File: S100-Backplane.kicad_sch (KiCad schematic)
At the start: 84 parts, among them IC1 7805, IC2 LM4250, IC3 PTN78000AAH, IC4 15V D30V30F15, IC5 7.5V D36V50F7, J1 Barrel_Jack_MountingPin, K1 CONN_3, P1 CONN_3X2, P10 CONN_1, P11 CONN_1, P12 CONN_2, P2 CONN_13X2, P3 CONN_13X2, P4 CONN_13X2, P5 CONN_13X2, P6 CONN_1, P7 CONN_1, P8 CONN_1, P9 CONN_1, Q1 2N3906TF, Q2 2N3904TA, Q3 TIP29BG, Q4 TIP30CG, SW1 SW_PUSH, SW2 B12JH, U31 S100_FEMALE, U32 S100_FEMALE, U33 S100_FEMALE, U34 S100_FEMALE, U35 S100_FEMALE, U36 S100_FEMALE, U37 S100_FEMALE, U38 S100_FEMALE, U39 S100_FEMALE

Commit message: Rev 1
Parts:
- removed F1, F2, F3: FUSE, R5, symbol S100-Backplane-rescue:FUSE
- removed JP1, JP2, JP3: JUMPER, SIL-2, symbol S100-Backplane-rescue:JUMPER
- removed R12, R13, R14: 270, R3, symbol S100-Backplane-rescue:R
- added D4: LED, S100 Backplane:LEDV, symbol S100-Backplane-rescue:LED
- added F1, F3: MF-R050-2, samac:MFR0502, symbol SamacSym:MF-R050-2
- added F2: MF-R250-2, samac:MFR2502, symbol SamacSym:MF-R250-2
- added JP1, JP2, JP3: Jumper_3_Open, Connector_PinHeader_2.54mm:PinHeader_1x03_P2.54mm_Vertical, symbol Jumper:Jumper_3_Open
- added JP4: ~, Connector_PinHeader_2.54mm:PinHeader_1x02_P2.54mm_Vertical, symbol Jumper:Jumper_2_Open
- added RR11: 270, Connector_PinHeader_2.54mm:PinHeader_1x05_P2.54mm_Vertical, symbol S100-Backplane-rescue:RR9
- R11: value 270 -> 27
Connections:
- net +18_V: now also F3.2
- net +8_V: now also F2.2
- net -16_V: now also F1.2
- net /CLOCK: now also RR11.3
- net /POC: now also RR11.5
- net F+16V: now also F3.1
- net F+8V: now also F2.1, JP4.2 (B); no longer C1.1, IC1.VI, Q1.1 (E), Q3.2, R5.1
- net F-16V: now also F1.1
- net GND: now also R11.2, JP1.3 (B), JP2.3 (B), JP3.3 (B)
- net PROT(GND): now also JP3.1 (A); no longer P3.16 (P16), U31.70 (0_V4), U32.70 (0_V4), U33.70 (0_V4), U34.70 (0_V4), U35.70 (0_V4), U36.70 (0_V4), U37.70 (0_V4), U38.70 (0_V4), U39.70 (0_V4)
- net SHLTA: now also RR11.2; no longer R11.1
- net SSTACK: now also RR11.4
- net UNPROT(T5): now also JP1.1 (A); no longer P3.15 (P15), U31.20 (0_V1), U32.20 (0_V1), U33.20 (0_V1), U34.20 (0_V1), U35.20 (0_V1), U36.20 (0_V1), U37.20 (0_V1), U38.20 (0_V1), U39.20 (0_V1)
- net Vacc: now also D4.1 (A), RR11.1 (COM); no longer R11.2
- net /SSW_DSBL renamed /J_SSW_DSBL
- net /J_SSW_DSBL: now also JP2.2 (C); no longer RR6.2
- new net: D4.2 (K), R11.1
- new net J_F+8V: C1.1, IC1.VI, JP4.1 (A), Q1.1 (E), Q3.2, R5.1
- new net J_PROT(GND): JP3.2 (C), P3.16 (P16), U31.70 (0_V4), U32.70 (0_V4), U33.70 (0_V4), U34.70 (0_V4), U35.70 (0_V4), U36.70 (0_V4), U37.70 (0_V4), U38.70 (0_V4), U39.70 (0_V4)
- new net J_UNPROT(T5): JP1.2 (C), P3.15 (P15), U31.20 (0_V1), U32.20 (0_V1), U33.20 (0_V1), U34.20 (0_V1), U35.20 (0_V1), U36.20 (0_V1), U37.20 (0_V1), U38.20 (0_V1), U39.20 (0_V1)
- new net /SSW_DSBL: JP2.1 (A), RR6.2
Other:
- moved on the sheet: C1, C2, C3, C4, C5, C6, C7, C8, D2, IC1, IC2, P10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

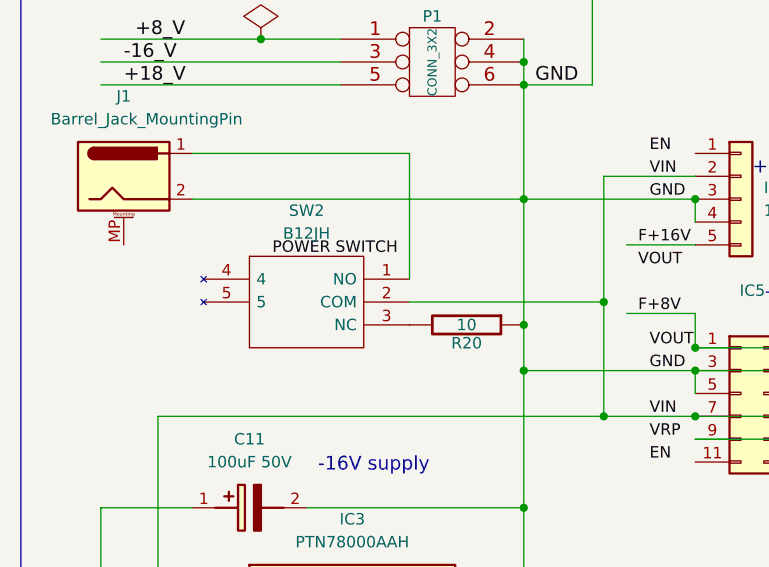
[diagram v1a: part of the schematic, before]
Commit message: R2
Updated SW2 power switch footprint to beefier part, E101MD1AQE.
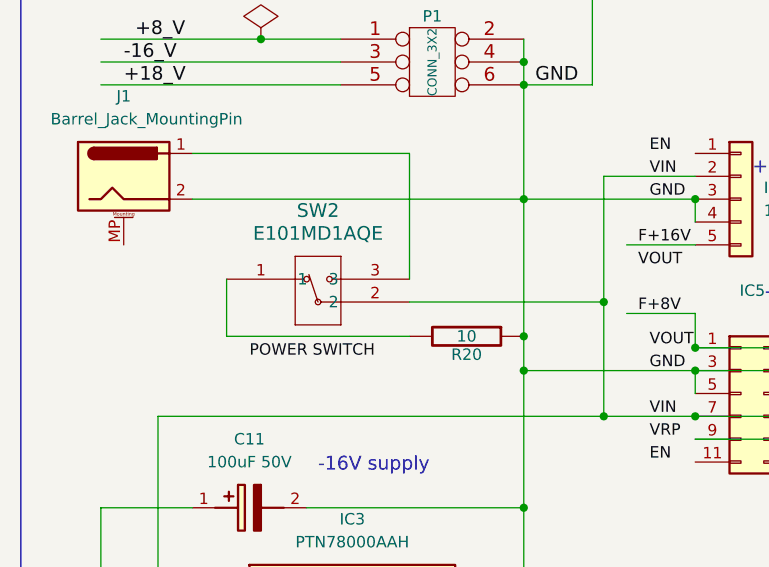
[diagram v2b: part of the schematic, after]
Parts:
- removed SW2: B12JH, B12JH, symbol SamacLib:B12JH
- added SW2: E101MD1AQE, SW_E1xxMD1AxE_CNK, symbol E101MD1AQE:E101MD1AQE
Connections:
- net VIN: now also SW2.2
- net at J1.1: now also SW2.3
- net at R20.2: now also SW2.1
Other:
- moved on the sheet: R20
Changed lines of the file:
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@@
   (junction (at 91.44 344.17) (diameter 0) (color 0 0 0 0)
   )
+  (junction (at 72.39 342.9) (diameter 0) (color 0 0 0 0)
+  )
   (junction (at 252.73 388.62) (diameter 0) (color 0 0 0 0)
   )
@@
   (junction (at 303.53 388.62) (diameter 0) (color 0 0 0 0)
   )
-  (junction (at 72.39 341.63) (diameter 0) (color 0 0 0 0)
-  )
   (junction (at 280.67 414.02) (diameter 0) (color 0 0 0 0)
   )
@@
     (stroke (width 0) (type default))
   )
-  (wire (pts (xy 72.39 341.63) (xy 72.39 346.71))
-    (stroke (width 0) (type default))
-  )
   (wire (pts (xy 332.74 99.06) (xy 351.79 99.06))
     (stroke (width 0) (type default))
@@
     (stroke (width 0) (type default))
   )
+  (wire (pts (xy 72.39 342.9) (xy 72.39 346.71))
+    (stroke (width 0) (type default))
+  )
   (wire (pts (xy 280.67 388.62) (xy 269.24 388.62))
     (stroke (width 0) (type default))
@@
     (stroke (width 0) (type default))
   )
-  (wire (pts (xy 72.39 327.66) (xy 72.39 341.63))
+  (wire (pts (xy 72.39 327.66) (xy 72.39 342.9))
     (stroke (width 0) (type default))
   )
@@
     (stroke (width 0) (type default))
   )
+  (wire (pts (xy 59.69 342.9) (xy 39.37 342.9))
+    (stroke (width 0) (type default))
+  )
   (wire (pts (xy 46.99 101.6) (xy 66.04 101.6))
     (stroke (width 0) (type default))
@@
     (stroke (width 0) (type default))
   )
+  (wire (pts (xy 39.37 342.9) (xy 39.37 336.55))
+    (stroke (width 0) (type default))
+  )
   (wire (pts (xy 165.1 233.68) (xy 184.15 233.68))
     (stroke (width 0) (type default))
@@
     (effects (font (size 1.524 1.524)) (justify left bottom))
   )
-  (label "POWER SWITCH" (at 44.45 334.01 0) (fields_autoplaced)
+  (label "POWER SWITCH" (at 41.91 345.44 0) (fields_autoplaced)
     (effects (font (size 1.27 1.27)) (justify left bottom))
   )
@@
     )
   )
-  (symbol (lib_id "SamacLib:B12JH") (at 36.83 336.55 0) (unit 1)
-    (in_bom yes) (on_board yes) (dnp no)
-    (property "Reference" "SW2" (at 48.26 328.93 0)
-      (effects (font (size 1.27 1.27)))
-    )
-    (property "Value" "B12JH" (at 48.26 331.47 0)
-      (effects (font (size 1.27 1.27)))
-    )
-    (property "Footprint" "B12JH" (at 55.88 334.01 0)
-      (effects (font (size 1.27 1.27)) (justify left) hide)
-    )
-    (property "Datasheet" "https://componentsearchengine.com/Datasheets/1/B12JH.pdf" (at 55.88 336.55 0)
-      (effects (font (size 1.27 1.27)) (justify left) hide)
-    )
-    (property "Description" "Toggle Switch IP65 SPDT On-None-On, 100 mA, PCB" (at 55.88 339.09 0)
-      (effects (font (size 1.27 1.27)) (justify left) hide)
-    )
-    (property "Height" "7.3" (at 55.88 341.63 0)
-      (effects (font (size 1.27 1.27)) (justify left) hide)
-    )
-    (property "Mouser Part Number" "633-B12JH" (at 55.88 344.17 0)
-      (effects (font (size 1.27 1.27)) (justify left) hide)
-    )
-    (property "Mouser Price/Stock" "https://www.mouser.co.uk/ProductDetail/NKK-Switches/B12JH?qs=44TLCAUTxJv3Lb2ZvYgQ9w%3D%3D" (at 55.88 346.71 0)
-      (effects (font (size 1.27 1.27)) (justify left) hide)
-    )
-    (property "Manufacturer_Name" "NKK Switches" (at 55.88 349.25 0)
-      (effects (font (size 1.27 1.27)) (justify left) hide)
-    )
-    (property "Manufacturer_Part_Number" "B12JH" (at 55.88 351.79 0)
-      (effects (font (size 1.27 1.27)) (justify left) hide)
-    )
-    (pin "1")
-    (pin "2")
-    (pin "3")
-    (pin "4")
-    (pin "5")
-    (instances
-      (project "S100-Backplane"
-        (path "/35e1b532-8c09-4997-b685-4f5b32c7c90b"
-          (reference "SW2") (unit 1)
-        )
-      )
-    )
-  )
   (symbol (lib_id "S100-Backplane-rescue:CONN_1") (at 33.02 290.83 0) (unit 1)
     (in_bom yes) (on_board yes) (dnp no)
@@
     )
   )
+  (symbol (lib_id "E101MD1AQE:E101MD1AQE") (at 39.37 336.55 0) (unit 1)
+    (in_bom yes) (on_board yes) (dnp no) (fields_autoplaced)
+    (property "Reference" "SW2" (at 49.53 328.93 0)
+      (effects (font (size 1.524 1.524)))
+    )
+    (property "Value" "E101MD1AQE" (at 49.53 331.47 0)
+      (effects (font (size 1.524 1.524)))
+    )
+    (property "Footprint" "SW_E1xxMD1AxE_CNK" (at 39.37 336.55 0)
+      (effects (font (size 1.27 1.27) italic) hide)
+    )
+    (property "Datasheet" "E101MD1AQE" (at 39.37 336.55 0)
+      (effects (font (size 1.27 1.27) italic) hide)
+    )
+    (pin "1")
+    (pin "2")
+    (pin "3")
+    (instances
+      (project "S100-Backplane"
+        (path "/35e1b532-8c09-4997-b685-4f5b32c7c90b"
+          (reference "SW2") (unit 1)
+        )
+      )
+    )
+  )
   (symbol (lib_id "SamacSys_Parts:ELXZ500ELL101MH12D") (at 31.75 391.16 0) (unit 1)
     (in_bom yes) (on_board yes) (dnp no) (fields_autoplaced)
@@
     )
   )
-  (symbol (lib_id "S100-Backplane-rescue:R") (at 66.04 341.63 270) (unit 1)
+  (symbol (lib_id "S100-Backplane-rescue:R") (at 66.04 342.9 270) (unit 1)
     (in_bom yes) (on_board yes) (dnp no)
-    (property "Reference" "R20" (at 66.04 343.662 90)
+    (property "Reference" "R20" (at 66.04 344.932 90)
       (effects (font (size 1.27 1.27)))
     )
-    (property "Value" "10" (at 66.04 341.63 90)
+    (property "Value" "10" (at 66.04 342.9 90)
       (effects (font (size 1.27 1.27)))
     )
-    (property "Footprint" "R3" (at 66.04 344.17 90)
+    (property "Footprint" "R3" (at 66.04 345.44 90)
       (effects (font (size 1.27 1.27)) hide)
     )
-    (property "Datasheet" "" (at 66.04 341.63 0)
+    (property "Datasheet" "" (at 66.04 342.9 0)
       (effects (font (size 1.27 1.27)) hide)
     )
